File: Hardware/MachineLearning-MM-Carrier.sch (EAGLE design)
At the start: 65 parts, among them J11 microSD, J2 JTAG, J3 QWIIC_RIGHT_ANGLE, J4 MICROMOD-2222-C, J7 CAMERA-HIMAX, U3 AP2127K-1.8V, U4 LIS2DH12, U5 AP7361C-33FGE

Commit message: Re-route camera connector for face up. Convert buzzard labels. Add power control to camera regulator.
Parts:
- removed D7: 1A/23V/620mV, SparkFun-DiscreteSemi:DIODE-SCHOTTKY-BAT20J
- removed JP4: JUMPER-SMT_2_NC_TRACE_SILK, SparkFun-Jumpers:JUMPER-SMT_2_NC_TRACE_SILK
- added 3V3_LED, VIN_LED: JUMPER-SMT_2_NC_TRACE_SILK, SparkFun-Jumpers:JUMPER-SMT_2_NC_TRACE_SILK
- added D3: BAS70-05, SparkFun-DiscreteSemi:DIODE-SCHOTTKY-DUAL
- added D4: Yellow, SparkFun-LED:LED-YELLOW0603
- added J9: (no value), SparkFun-Connectors:CONN_01PTH_NO_SILK_YES_STOP
- added R6: 4.7k, SparkFun-Resistors:4.7KOHM-0603-1/10W-1%
- added VE: JUMPER-SMT_2_NO_SILK, SparkFun-Jumpers:JUMPER-SMT_2_NO_SILK
- J5: value (none) -> SPI
- J6: value (none) -> UART
- J7: value CAMERA-HIMAX -> CAMERA-HIMAXFACEUP; device SparkFun-Connectors:CAMERA-HIMAX -> SparkFun-Connectors:CAMERA-HIMAXFACEUP
- J8: value (none) -> Dedicated
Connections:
- net HEADER_!CS! renamed D0/HEADER_!CS!
- net N$1 renamed VREG_3.3V
- net SD_DAT1 renamed SDIO_DAT1
- net SD_DAT2 renamed SDIO_DAT2
- removed net PWM1: J4.PWM1, J8.4
- removed net SD_!CS!: J11.DAT3/CS, J4.SPI_!CS!/SDIO_DATA3
- removed net SPI_MISO: J11.DAT0/MISO, J4.SPI_MISO/SDIO_DATA0, J5.3
- removed net SPI_MOSI: J11.CMD/MOSI, J4.SPI_MOSI/SDIO_CMD, J5.2
- new net N$1: R6.2, VIN_LED.1
- new net N$12: D1.C, R5.1, U5.EN, VE.2
- new net N$8: D4.A, R6.1
- new net PWM1/CAM_VDD: J4.PWM1, J8.4, U3.EN
- new net SPI_!CS!/SDIO_DAT3: J11.DAT3/!CS!, J4.SPI_!CS!/SDIO_DATA3
- new net SPI_SDI: J11.DAT0/SDO, J4.SPI_SDI/SDIO_DATA0, J5.3
- new net SPI_SDO: J11.CMD/SDI, J4.SPI_SDO/SDIO_CMD, J5.2
- net !RESET!: now also J9.1
- net 3.3V: now also 3V3_LED.2, D3.A1; no longer D7.A, JP4.2, U3.EN
- net 3.3V_EN: now also VE.1; no longer D1.C, R5.1, U5.EN
- net GND: now also D4.C
- net N$6: now also 3V3_LED.1; no longer JP4.1
- net RTC_3V: now also D3.C; no longer D7.C
- net VIN: now also VIN_LED.2
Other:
- note added: "0.100uA Leakage 0.410V drop at 1mA 1.0V drop at 15mA"
- note added: "Be careful providing external 3.3V here as it may compete with the 3.3V regulator."
- note added: "Close VE to enable processor control of 3.3V bus."
- note added: "Closing jumper bypasses PTC to allow >2A current flows."
- note added: "MicroMod Connector"
- note added: "N. Seidle"
- note added: "VIN: 3.7-6.0V"
- note added: "v12"
- note removed: "0.65uA Leakage 0.3V drop at 10mA"
- note removed: "This is the penny-in-the-fuse jumper. Close only if you know what you're doing."
- note removed: "Universal MicroMod Connector"
- moved on the sheet: BYP, C1, C13, C2, C22, C3, C4, C5, D1, D2, F2, J7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

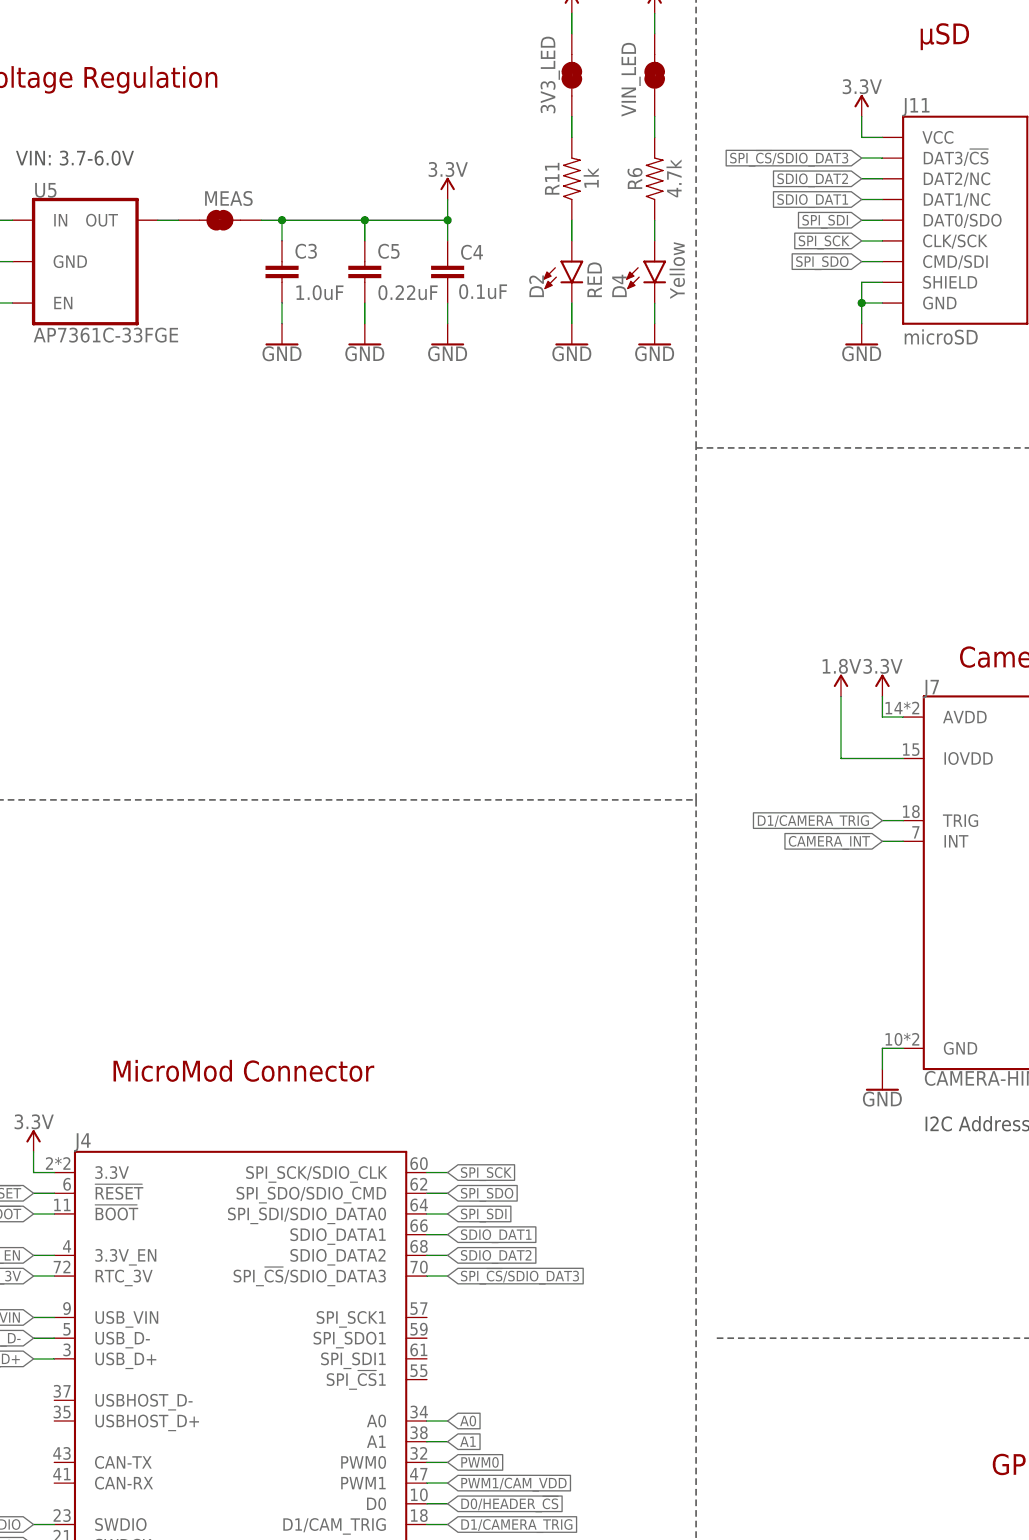
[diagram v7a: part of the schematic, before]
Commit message: Update MicroMod connector with SPI port changes
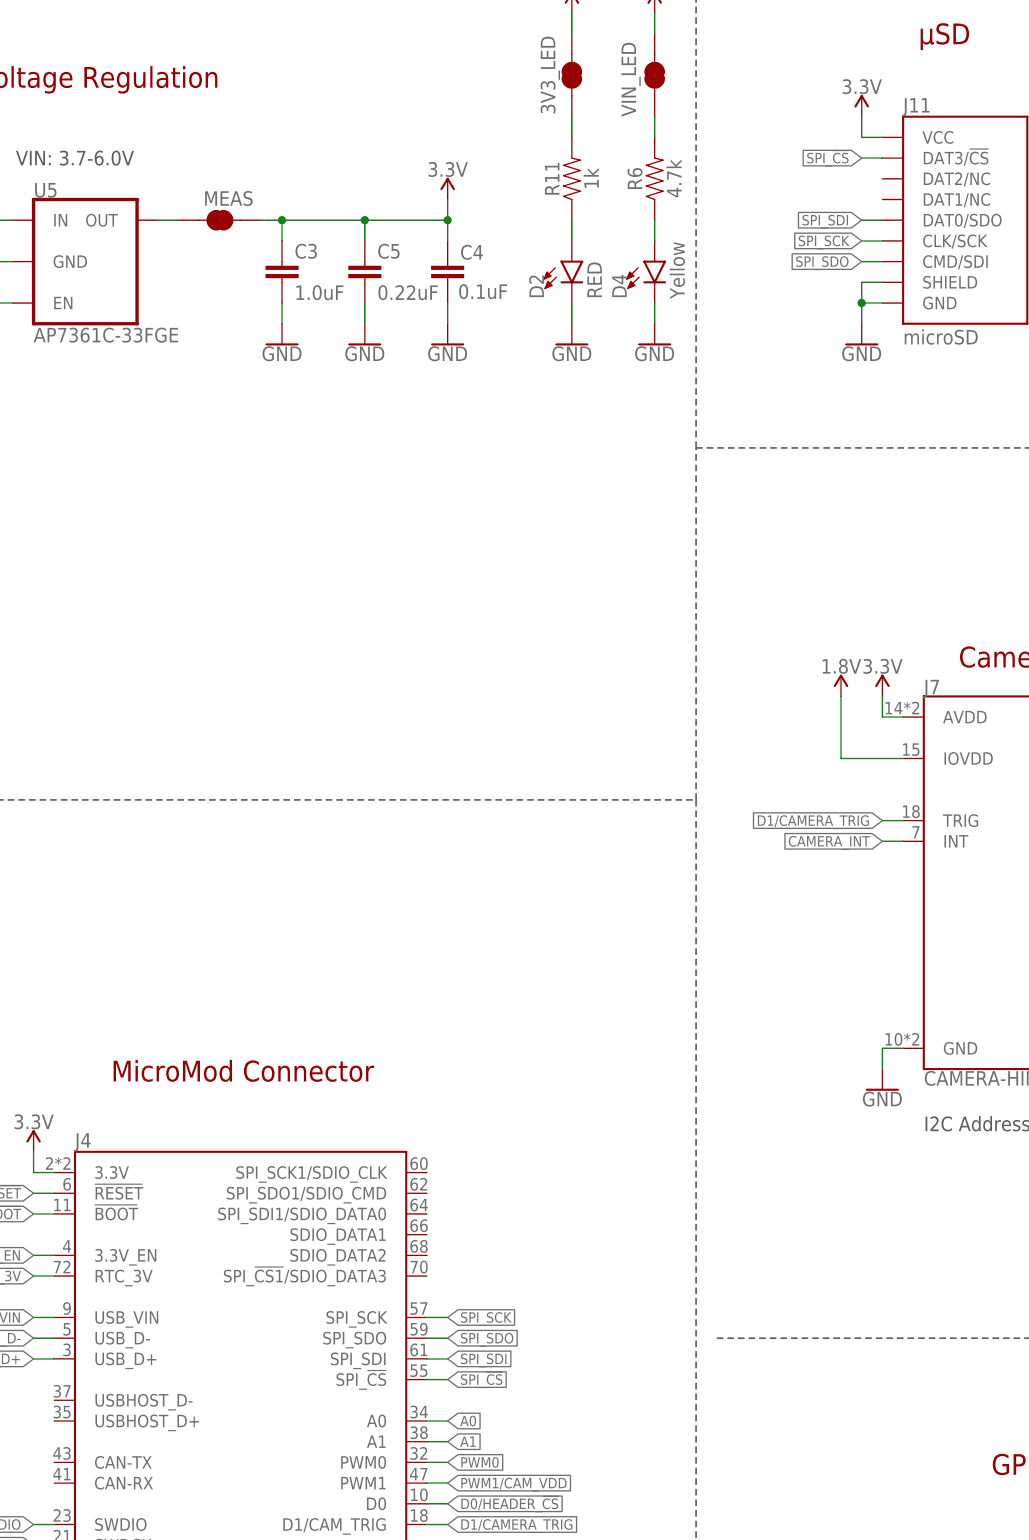
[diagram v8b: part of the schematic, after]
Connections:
- removed net SDIO_DAT1: J11.DAT1/NC, J4.SDIO_DATA1
- removed net SDIO_DAT2: J11.DAT2/NC, J4.SDIO_DATA2
- removed net SPI_!CS!/SDIO_DAT3: J11.DAT3/!CS!, J4.SPI_!CS!/SDIO_DATA3
- new net SPI_!CS!: J11.DAT3/!CS!, J4.SPI_!CS!
- net SPI_SCK: now also J4.SPI_SCK; no longer J4.SPI_SCK/SDIO_CLK
- net SPI_SDI: now also J4.SPI_SDI; no longer J4.SPI_SDI/SDIO_DATA0
- net SPI_SDO: now also J4.SPI_SDO; no longer J4.SPI_SDO/SDIO_CMD
